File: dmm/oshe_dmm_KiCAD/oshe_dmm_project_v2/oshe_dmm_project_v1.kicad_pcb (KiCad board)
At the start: 4 copper layers, 88.9 x 165.1 mm, 76 parts, among them J1 FTDI Basic, J10 Voltage Range 2, J11 Voltage Range 3, J12 Voltage Range 3, J13 Current Indication, J2 Voltage, J3 GND, J4 Current, J5 Resistance Meas, J6 ON/OFF, J7 Voltage Range 1, J8 Voltage Range 1, J9 Voltage Range 2, SW1 PTS526 SK15 SMTR2 LFS, U1 ATmega328P-A, U3 ADS1115IDGS, U4 MAX4617CPE, U5 LM317_SOT-223, Y1 16MHz

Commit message: Updated PCB
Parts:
- added J14: Continuity, Connector_PinHeader_2.54mm:PinHeader_1x02_P2.54mm_Vertical, F.Cu at (232.9, 121.9)
- added J15: AC Voltage Range 2, Connector_PinHeader_2.54mm:PinHeader_1x02_P2.54mm_Vertical, F.Cu at (228.6, 167.0)
- added J16: AC Voltage Range 2, Connector_PinHeader_2.54mm:PinHeader_1x02_P2.54mm_Vertical, F.Cu at (233.2, 167.0)
- added J17: AC Voltage Range 3, Connector_PinHeader_2.54mm:PinHeader_1x02_P2.54mm_Vertical, F.Cu at (237.8, 167.0)
- added J18: AC Voltage Range 3, Connector_PinHeader_2.54mm:PinHeader_1x02_P2.54mm_Vertical, F.Cu at (242.4, 167.0)
- added J19: AC Voltage Range 1, Connector_PinHeader_2.54mm:PinHeader_1x02_P2.54mm_Vertical, F.Cu at (261.9, 165.7)
- added J20: AC Voltage Range 1, Connector_PinHeader_2.54mm:PinHeader_1x02_P2.54mm_Vertical, F.Cu at (244.7, 190.6)
- added J21: AC Current Indication, Connector_PinHeader_2.54mm:PinHeader_1x02_P2.54mm_Vertical, F.Cu at (265.7, 180.3)
- added R36: R?, Resistor_SMD:R_1206_3216Metric_Pad1.30x1.75mm_HandSolder, F.Cu at (229.3, 173.5)
- added R37: R?, Resistor_SMD:R_1206_3216Metric_Pad1.30x1.75mm_HandSolder, F.Cu at (245.0, 177.5)
- added R38: R?, Resistor_SMD:R_1206_3216Metric_Pad1.30x1.75mm_HandSolder, F.Cu at (235.6, 193.3)
- added R39: R?, Resistor_SMD:R_1206_3216Metric_Pad1.30x1.75mm_HandSolder, F.Cu at (257.8, 189.0)
- added R8: 1k, Resistor_SMD:R_1206_3216Metric_Pad1.30x1.75mm_HandSolder, F.Cu at (147.7, 179.8)
- added R9: R?, Resistor_SMD:R_1206_3216Metric_Pad1.30x1.75mm_HandSolder, F.Cu at (238.2, 124.6)
- C9: footprint Connector_PinHeader_2.54mm:PinHeader_1x02_P2.54mm_Vertical -> Capacitor_THT:CP_Radial_D6.3mm_P2.50mm
- J13: value Current Indication -> DC Current Indication
- moved D4 12.1 mm to (201.2, 140.2), turned to 90 degrees
- moved DS1 12.0 mm to (132.5, 74.2)
- moved R14 11.6 mm to (148.8, 113.4)
- moved RV1 11.6 mm to (138.1, 113.4)
- moved F2 11.3 mm to (184.5, 210.4), turned to 90 degrees
- moved C9 10.8 mm to (124.0, 134.8)
- moved R18 6.94 mm to (143.3, 150.7)
- moved R21 6.94 mm to (135.6, 150.6)
- moved R31 6.94 mm to (135.6, 135.8)
- moved R33 6.94 mm to (138.2, 135.8)
- moved U4 6.94 mm to (136.9, 143.3)
- moved R16 6.94 mm to (138.2, 150.7)
- moved R17 6.94 mm to (140.7, 150.7)
- moved R30 6.94 mm to (145.8, 135.5)
- moved R32 6.94 mm to (143.2, 135.8)
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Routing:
- net GND: track 232.5 -> 51.4 mm, vias 25 -> 23
- net Net-(J13-Pin_2): track 61.2 -> 106.6 mm, vias 3 -> 5
- net 2V_Rang: track 141.9 -> 164.3 mm
- net 200V_Rang: track 65.3 -> 79.1 mm
- net Net-(J10-Pin_2): track 75.8 -> 88.5 mm
- net Net-(J8-Pin_2): track 89.5 -> 101.9 mm, vias 5 -> 3
- net D2: track 101.2 -> 113.3 mm
- net MOSI/D11: track 103.0 -> 115.0 mm
- net MISO/D12: track 103.5 -> 115.5 mm
- net D5: track 109.0 -> 121.0 mm
- net D3: track 100.7 -> 112.7 mm
- net D4: track 100.6 -> 112.6 mm
- net 20V_Rang: track 77.7 -> 89.5 mm
- net Net-(J12-Pin_2): track 61.5 -> 73.3 mm
- net V_ADC_Input: track 110.9 -> 122.7 mm
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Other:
- board text added: "200VAC"
- board text added: "200VDC"
- board text added: "20VAC"
- board text added: "20VDC"
- board text added: "2VAC"
- board text added: "2VDC"
- board text added: "CONTINUITY"
- board text added: "DCI"
- board text added: "RESIST"

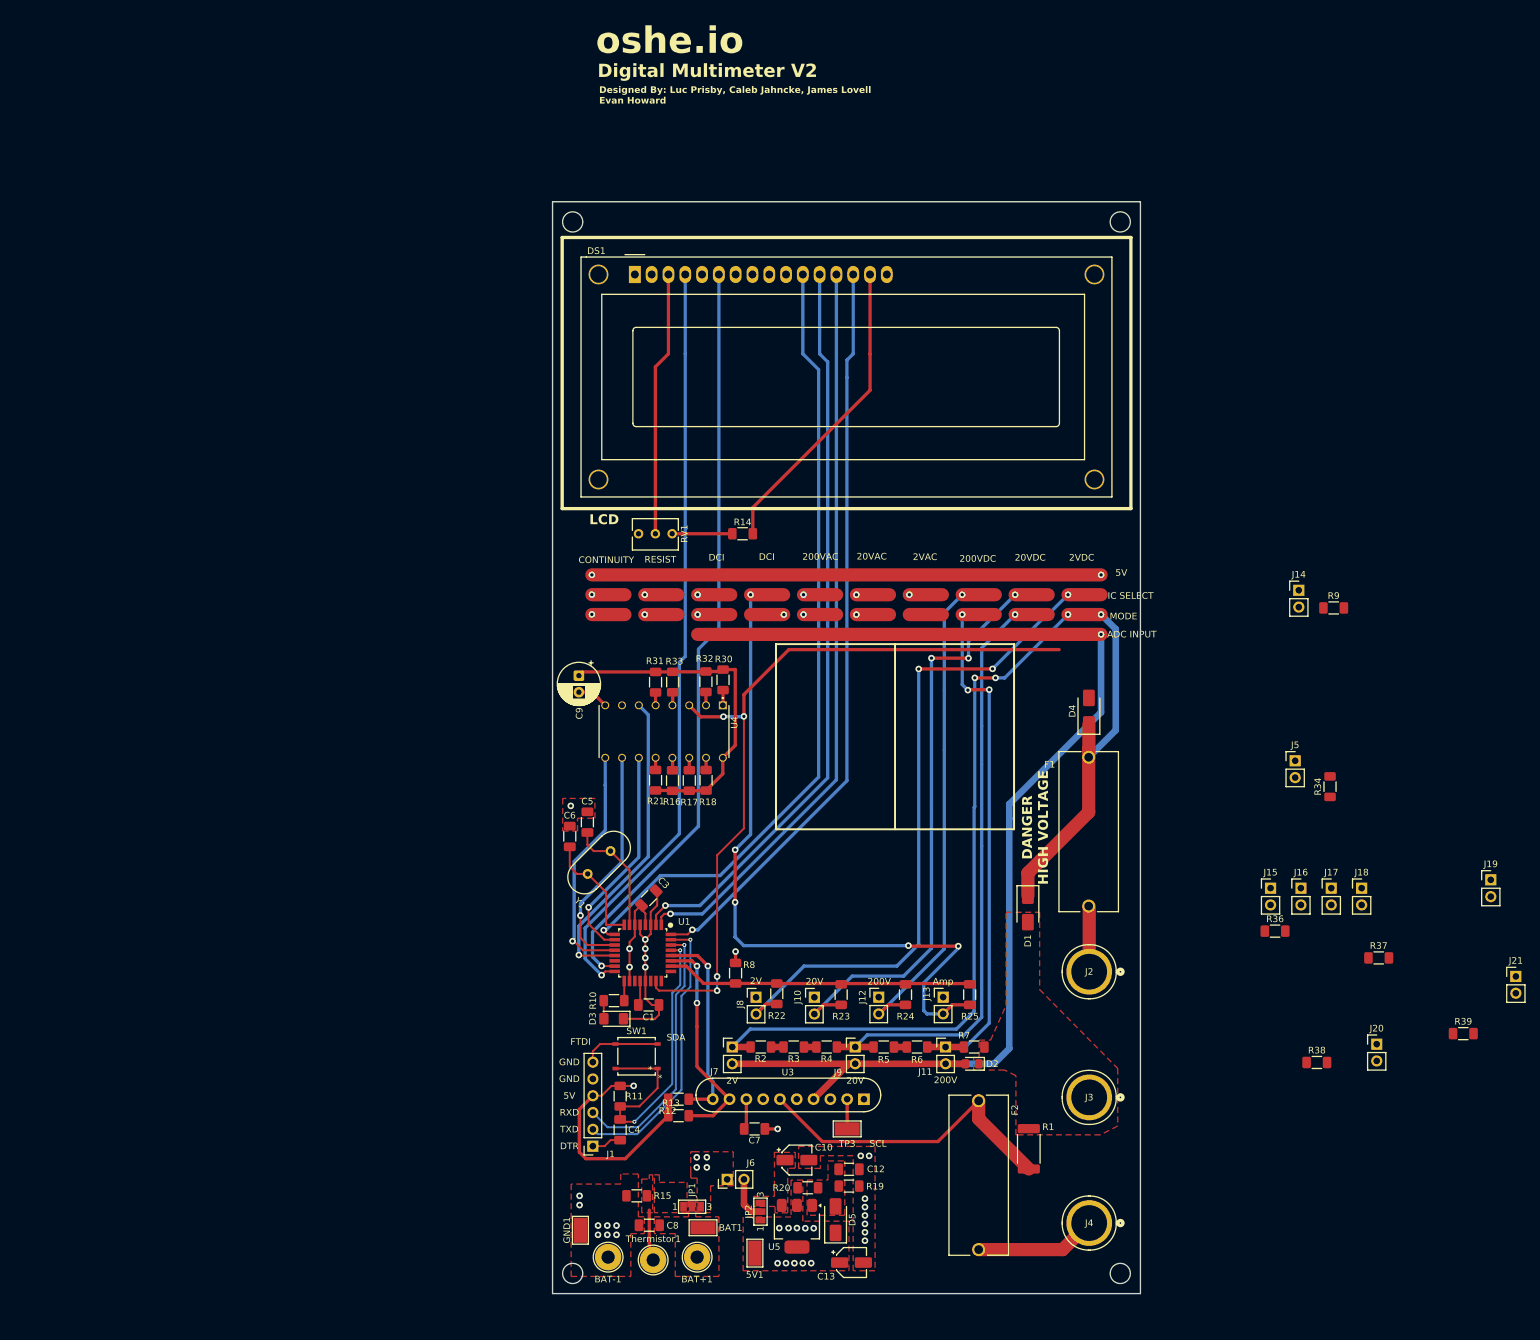
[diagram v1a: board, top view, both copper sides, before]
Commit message: AC current and voltage measurement
Updated Schematic and PCB to include AC voltage and current measurement. Also fixed an issue with DC voltage and current ADC had the wrong pin numbers assigned.
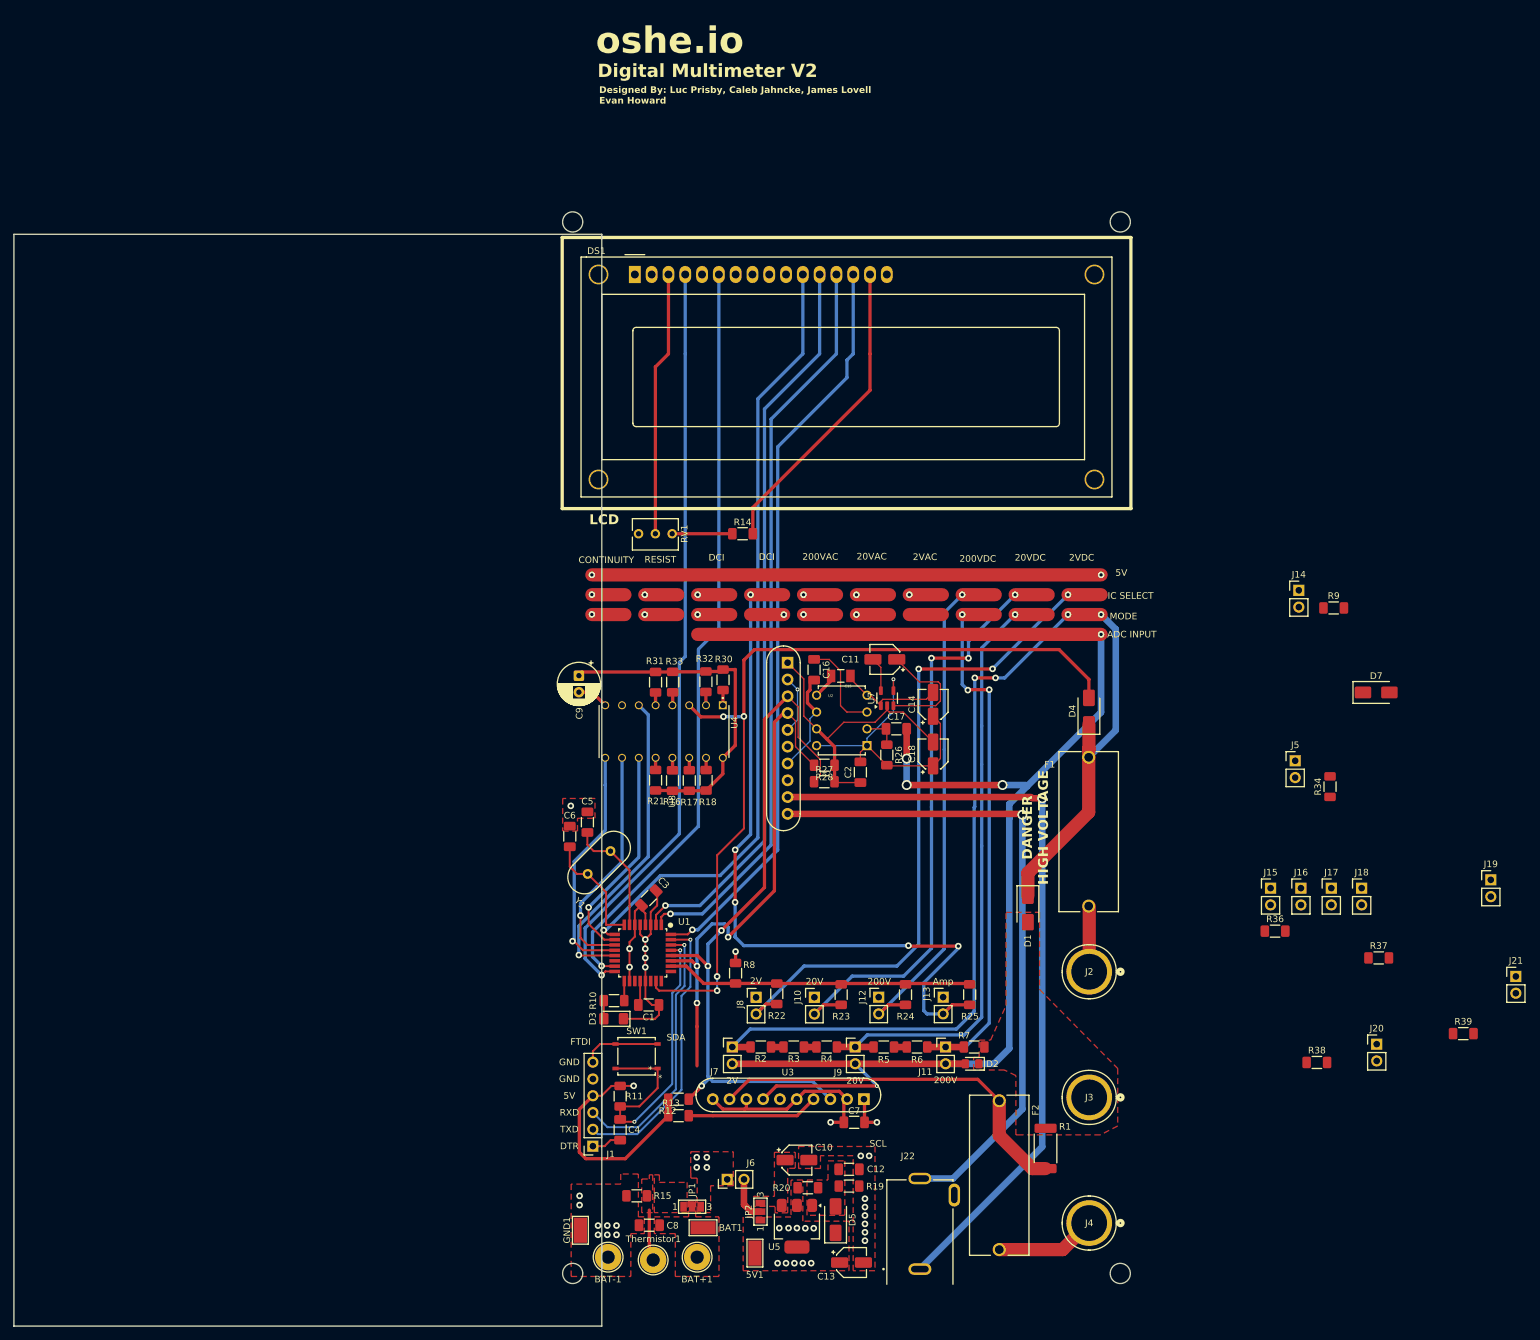
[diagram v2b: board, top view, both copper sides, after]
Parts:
- removed TP3: ALERT, TestPoint:TestPoint_Keystone_5019_Minature
- added C11: 1uF, Capacitor_SMD:CP_Elec_4x4.5, F.Cu at (170.3, 132.4)
- added C14: 1uF, Capacitor_SMD:CP_Elec_4x4.5, F.Cu at (177.6, 139.2)
- added C15: 100uF, footprints:CAPC3216X190N, F.Cu at (163.6, 134.9)
- added C16: 10uF, Capacitor_SMD:C_1206_3216Metric_Pad1.33x1.80mm_HandSolder, F.Cu at (159.6, 133.9)
- added C17: 10uF, Capacitor_SMD:C_1206_3216Metric_Pad1.33x1.80mm_HandSolder, F.Cu at (172.0, 142.9)
- added C18: 1uF, Capacitor_SMD:CP_Elec_4x4.5, F.Cu at (177.6, 146.7)
- added C2: 0.1uF, Capacitor_SMD:C_1206_3216Metric_Pad1.33x1.80mm_HandSolder, F.Cu at (166.6, 149.4)
- added D7: SMAJ200A, Diode_SMD:D_SMA, F.Cu at (244.6, 137.4)
- added J22: MJ-3536N, footprints:SAMESKY_MJ-3536N, F.Cu at (175.6, 224.6)
- added R26: 1M, Resistor_SMD:R_1206_3216Metric_Pad1.30x1.75mm_HandSolder, F.Cu at (170.6, 146.8)
- added R27: 10k, Resistor_SMD:R_1206_3216Metric_Pad1.30x1.75mm_HandSolder, F.Cu at (161.1, 150.9)
- added R28: 10k, Resistor_SMD:R_1206_3216Metric_Pad1.30x1.75mm_HandSolder, F.Cu at (161.1, 148.4)
- added U2: AD736, footprints:PDIP-8_N, F.Cu at (160.0, 137.8)
- added U7: TPS60400DBV, Package_TO_SOT_SMD:SOT-23-5, F.Cu at (170.6, 138.2)
- added U8: ADS1115IDGS, ZC261500:MODULE_ZC261500, F.Cu at (148.9, 144.3)
- R22: value 390 -> 180
- R23: value 1k -> 680
- R24: value 1.78k -> 1.2k
- R25: value 3.3k -> R?
- R36: value R? -> 2.4k
- R37: value R? -> 3k
- R38: value R? -> 1.8k
- moved C7 15.1 mm to (165.7, 202.4), turned to 0 degrees
- moved F2 3.11 mm to (187.6, 210.4)
- moved R1 2.53 mm to (194.6, 206.3)
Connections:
- J15 pad 1: 20V_AC_Rang -> 20V_Rang
- J17 pad 1: 200V_AC_Rang -> 200V_Rang
- J19 pad 1: 2V_AC_Rang -> 2V_Rang
- U3 pad 1: GND -> +5V
- U3 pad 10: SCL -> GND
- U3 pad 2: Net-(U3-ALERT/RDY) -> GND
- U3 pad 3: GND -> SCL
- U3 pad 4: V_ADC_Input -> SDA
- U3 pad 6: Net-(U3-AIN2) -> Net-(U3-ALERT/RDY)
- U3 pad 7: GND -> V_ADC_Input
- U3 pad 8: +5V -> GND
- U3 pad 9: SDA -> Net-(U3-AIN2)
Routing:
- net Net-(U8-AIN2): track 0.00 -> 117.4 mm, vias 0 -> 1
- net Net-(U8-AIN3): track 0.00 -> 99.9 mm, vias 0 -> 1
- net GND: track 51.4 -> 131.4 mm, vias 23 -> 25
- net SCL: track 30.3 -> 109.1 mm, vias 1 -> 3
- net SDA: track 33.7 -> 98.4 mm, vias 2 -> 3
- net +5V: track 115.6 -> 161.8 mm, vias 15 -> 14
- net V_ADC_Input: track 122.7 -> 164.7 mm, vias 1 -> 5
- net Net-(U7-C_{FLY-}): track 0.00 -> 18.1 mm
- net Net-(U2--Vs): track 0.00 -> 15.9 mm
- net Net-(U2-OUTPUT): track 0.00 -> 15.6 mm
- net Net-(U2-Cf): track 0.00 -> 14.4 mm
- net A0: track 116.7 -> 128.9 mm
- net Net-(U3-AIN2): track 48.7 -> 57.7 mm
- net Net-(U2-Vin): track 0.00 -> 5.33 mm
- net Net-(U7-C_{FLY+}): track 0.00 -> 5.22 mm
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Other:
- board size 88.9 x 165.1 mm -> 168.8 x 168.5 mm

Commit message: changes PCB
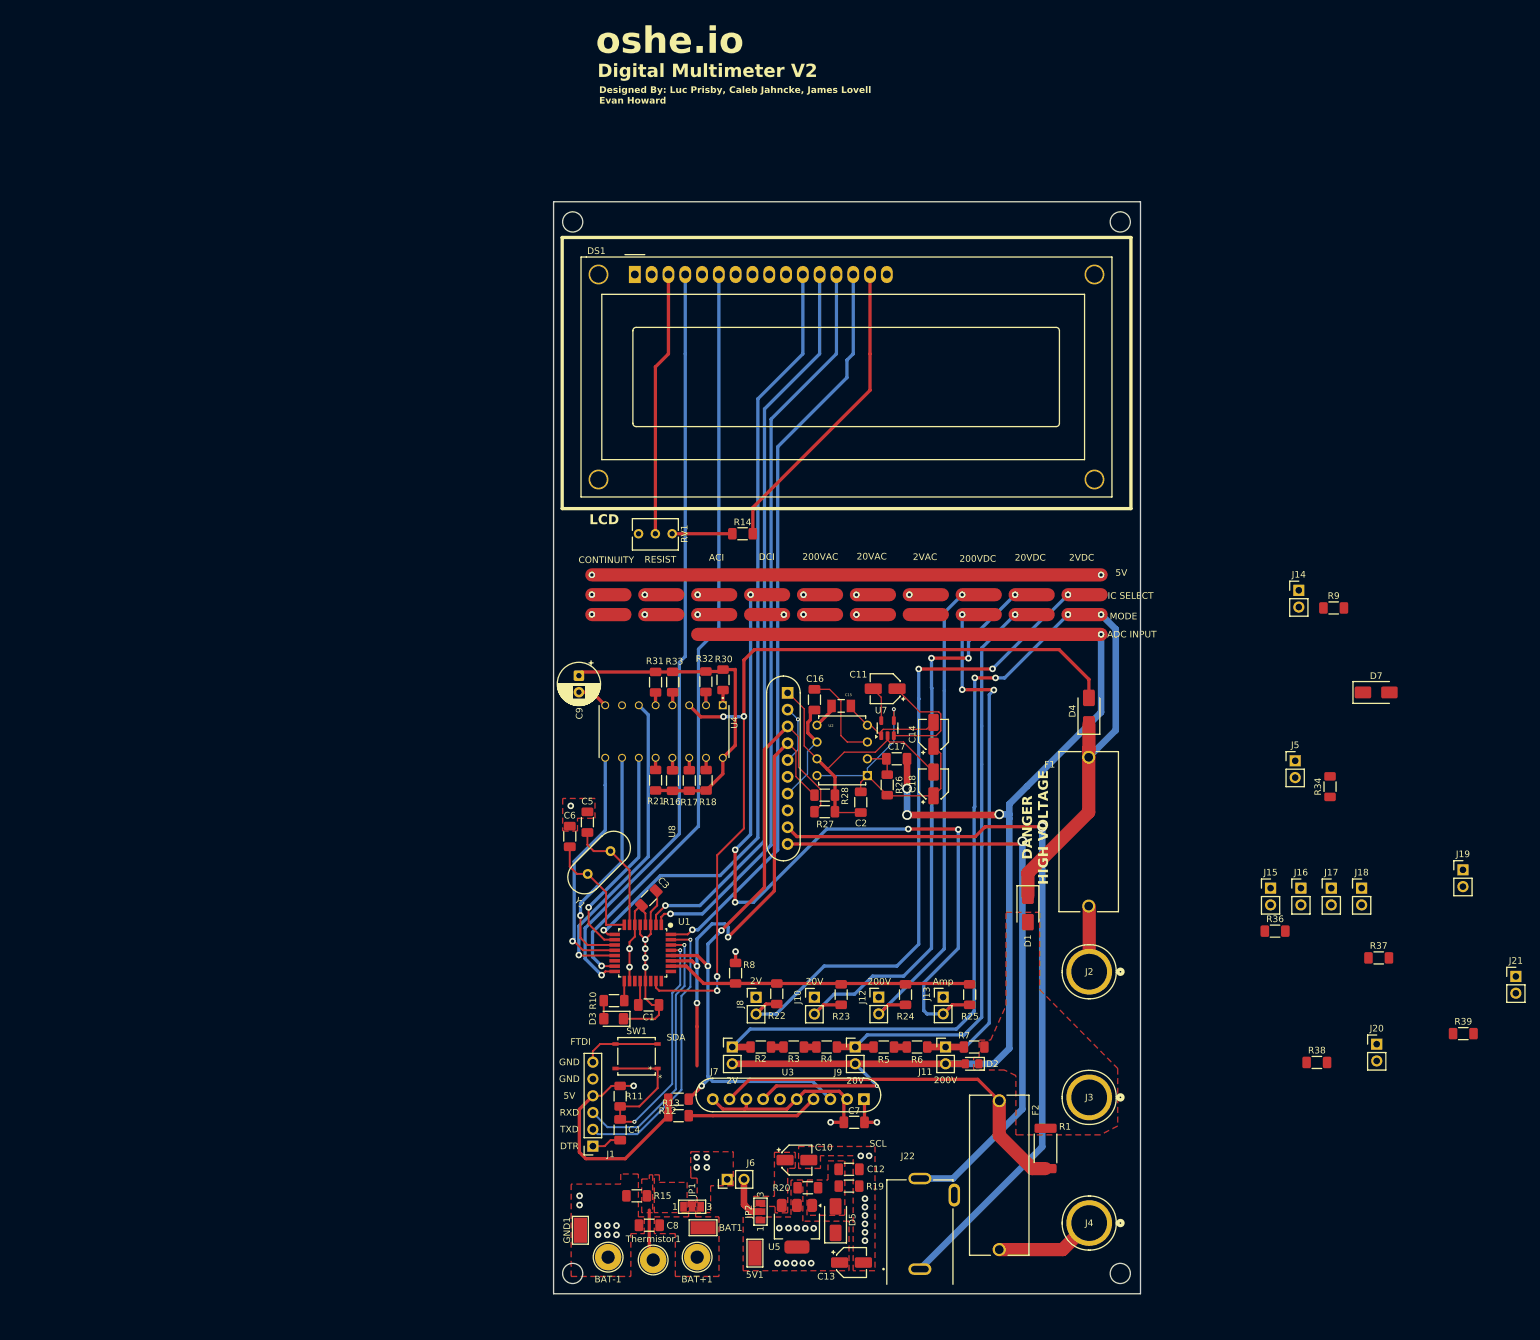
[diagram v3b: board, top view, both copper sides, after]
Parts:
- moved U8 4.56 mm to (148.9, 148.9)
- moved C14 4.53 mm to (177.7, 143.7)
- moved C15 4.53 mm to (163.7, 139.4)
- moved C16 4.53 mm to (159.7, 138.5)
- moved C17 4.53 mm to (172.1, 147.4)
- moved C18 4.53 mm to (177.7, 151.2)
- moved C2 4.53 mm to (166.7, 154.0)
- moved R26 4.53 mm to (170.7, 151.4)
- moved R27 4.53 mm to (161.2, 155.4)
- moved R28 4.53 mm to (161.2, 152.9)
- moved U2 4.53 mm to (160.0, 142.3)
- moved U7 4.53 mm to (170.7, 142.8)
- moved J19 4.47 mm to (257.7, 164.2)
- moved C11 4.43 mm to (170.3, 136.8)
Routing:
- net Net-(J13-Pin_2): track 106.6 -> 123.4 mm
- net SCL: track 109.1 -> 104.6 mm
- net Net-(J10-Pin_2): track 88.5 -> 93.0 mm
- net SDA: track 98.4 -> 94.1 mm
- net Net-(U8-AIN3): track 99.9 -> 96.0 mm
- net Net-(U8-AIN2): track 117.4 -> 114.3 mm
- net V_ADC_Input: track 164.7 -> 162.2 mm
- net 200V_Rang: track 79.1 -> 81.2 mm
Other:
- board size 168.8 x 168.5 mm -> 88.7 x 165.1 mm
- board text added: "ACI"

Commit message: Finalished PCB
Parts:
- removed J15: AC Voltage Range 2, Connector_PinHeader_2.54mm:PinHeader_1x02_P2.54mm_Vertical
- removed J17: AC Voltage Range 3, Connector_PinHeader_2.54mm:PinHeader_1x02_P2.54mm_Vertical
- removed J19: AC Voltage Range 1, Connector_PinHeader_2.54mm:PinHeader_1x02_P2.54mm_Vertical
- removed R27, R28: 10k, Resistor_SMD:R_1206_3216Metric_Pad1.30x1.75mm_HandSolder
- moved J21 104.9 mm to (161.3, 170.9)
- moved R9 102.2 mm to (151.2, 178.2), turned to 90 degrees
- moved R39 97.1 mm to (161.3, 177.9), turned to 90 degrees
- moved J14 93.0 mm to (153.7, 170.8)
- moved R34 84.3 mm to (157.5, 177.9)
- moved R37 79.2 mm to (165.7, 177.9), turned to 90 degrees
- moved J5 78.3 mm to (157.5, 170.8)
- moved J18 76.7 mm to (165.8, 170.8)
- moved J20 73.2 mm to (174.2, 170.8)
- moved D7 66.6 mm to (183.8, 164.8), turned to 180 degrees
- moved J16 63.2 mm to (170.1, 170.8)
- moved R38 61.7 mm to (175.9, 177.8), turned to 90 degrees
- moved R36 59.3 mm to (170.1, 177.9), turned to 90 degrees
- moved C11 1.91 mm to (168.6, 136.0)
- moved R14 1.77 mm to (148.8, 111.6)
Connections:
- D7 pad 2: A1 -> D10
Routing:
- net Net-(J14-Pin_2): track 0.00 -> 103.4 mm, vias 0 -> 3
- net Net-(J5-Pin_2): track 0.00 -> 93.4 mm, vias 0 -> 3
- net Net-(J21-Pin_2): track 0.00 -> 92.3 mm, vias 0 -> 3
- net D10: track 0.00 -> 83.8 mm, vias 0 -> 4
- net Net-(J18-Pin_2): track 0.00 -> 59.2 mm, vias 0 -> 1
- net Net-(J20-Pin_2): track 0.00 -> 56.9 mm, vias 0 -> 1
- net Net-(J16-Pin_2): track 0.00 -> 55.2 mm, vias 0 -> 1
- net GND: track 131.4 -> 88.7 mm
- net 2V_Rang: track 164.3 -> 202.4 mm, vias 4 -> 5
- net 20V_Rang: track 89.5 -> 114.8 mm, vias 1 -> 2
- net 200V_Rang: track 81.2 -> 106.4 mm, vias 3 -> 4
- net SDA: track 94.1 -> 107.2 mm
- net A3: track 46.2 -> 57.7 mm
- net Net-(U7-C_{FLY-}): track 18.1 -> 20.2 mm
- net A0: track 128.9 -> 130.7 mm, vias 4 -> 5
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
